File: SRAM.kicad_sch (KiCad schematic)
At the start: 5 parts, among them U1301 23LC1024-I/SN

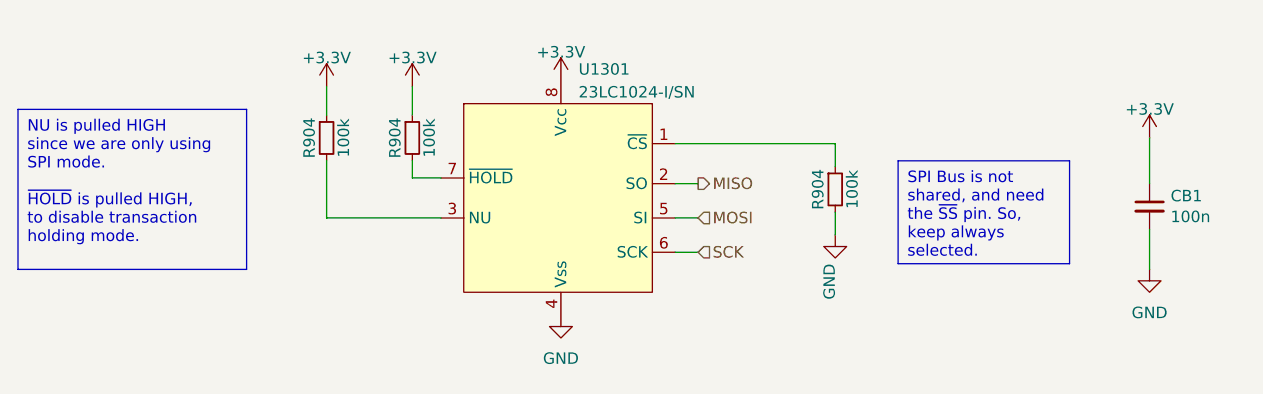
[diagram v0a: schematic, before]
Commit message: (pcb) route power
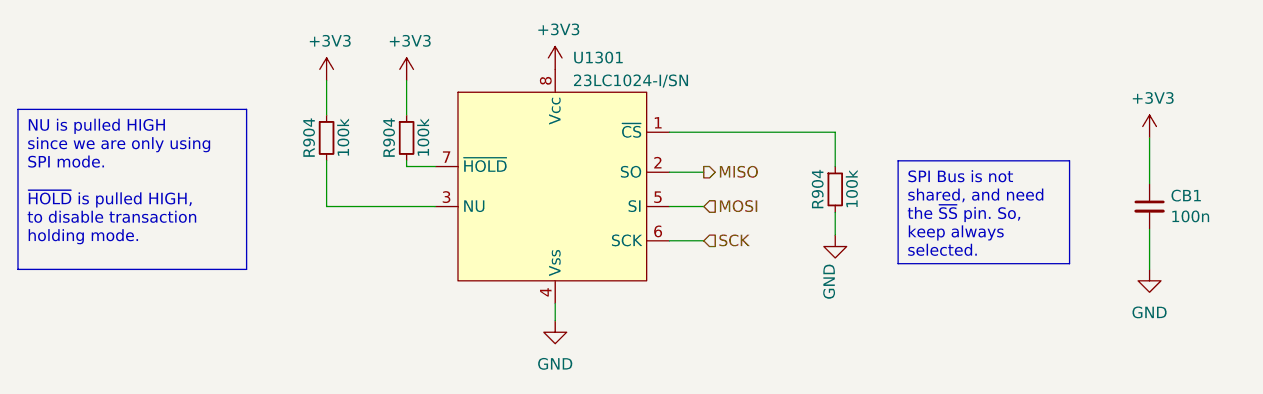
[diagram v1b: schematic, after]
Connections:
- net +3.3V renamed +3V3
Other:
- moved on the sheet: R904, U1301

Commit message: (sch) consoldate BOM
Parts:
- U1301: MPN (none) -> 23LC1024-I/SN; Mfr. (none) -> Microchip Technology
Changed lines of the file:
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@@
+      (effects (font (size 1.27 1.27)) hide)
+    )
+    (property "MPN" "23LC1024-I/SN" (at 116.84 101.6 0)
+      (effects (font (size 1.27 1.27)) hide)
+    )
+    (property "Mfr." "Microchip Technology" (at 116.84 101.6 0)
       (effects (font (size 1.27 1.27)) hide)
     )

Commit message: chore: update kicad version
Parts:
- renumbered CB1 to CB1301, R904 to R1301, R904 to R1302, R904 to R1303
